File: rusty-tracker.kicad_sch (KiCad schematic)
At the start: 174 parts, among them J1 SIM8051-6-0-14-01-X, J2 USB_C_Receptacle_USB2.0, J3 NFC, J4 tag-connect-swd, J5 Battery Connector, Q1 BC846, Q2 BC846, SW1 SW_Push, T1 Tab, T2 Tab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

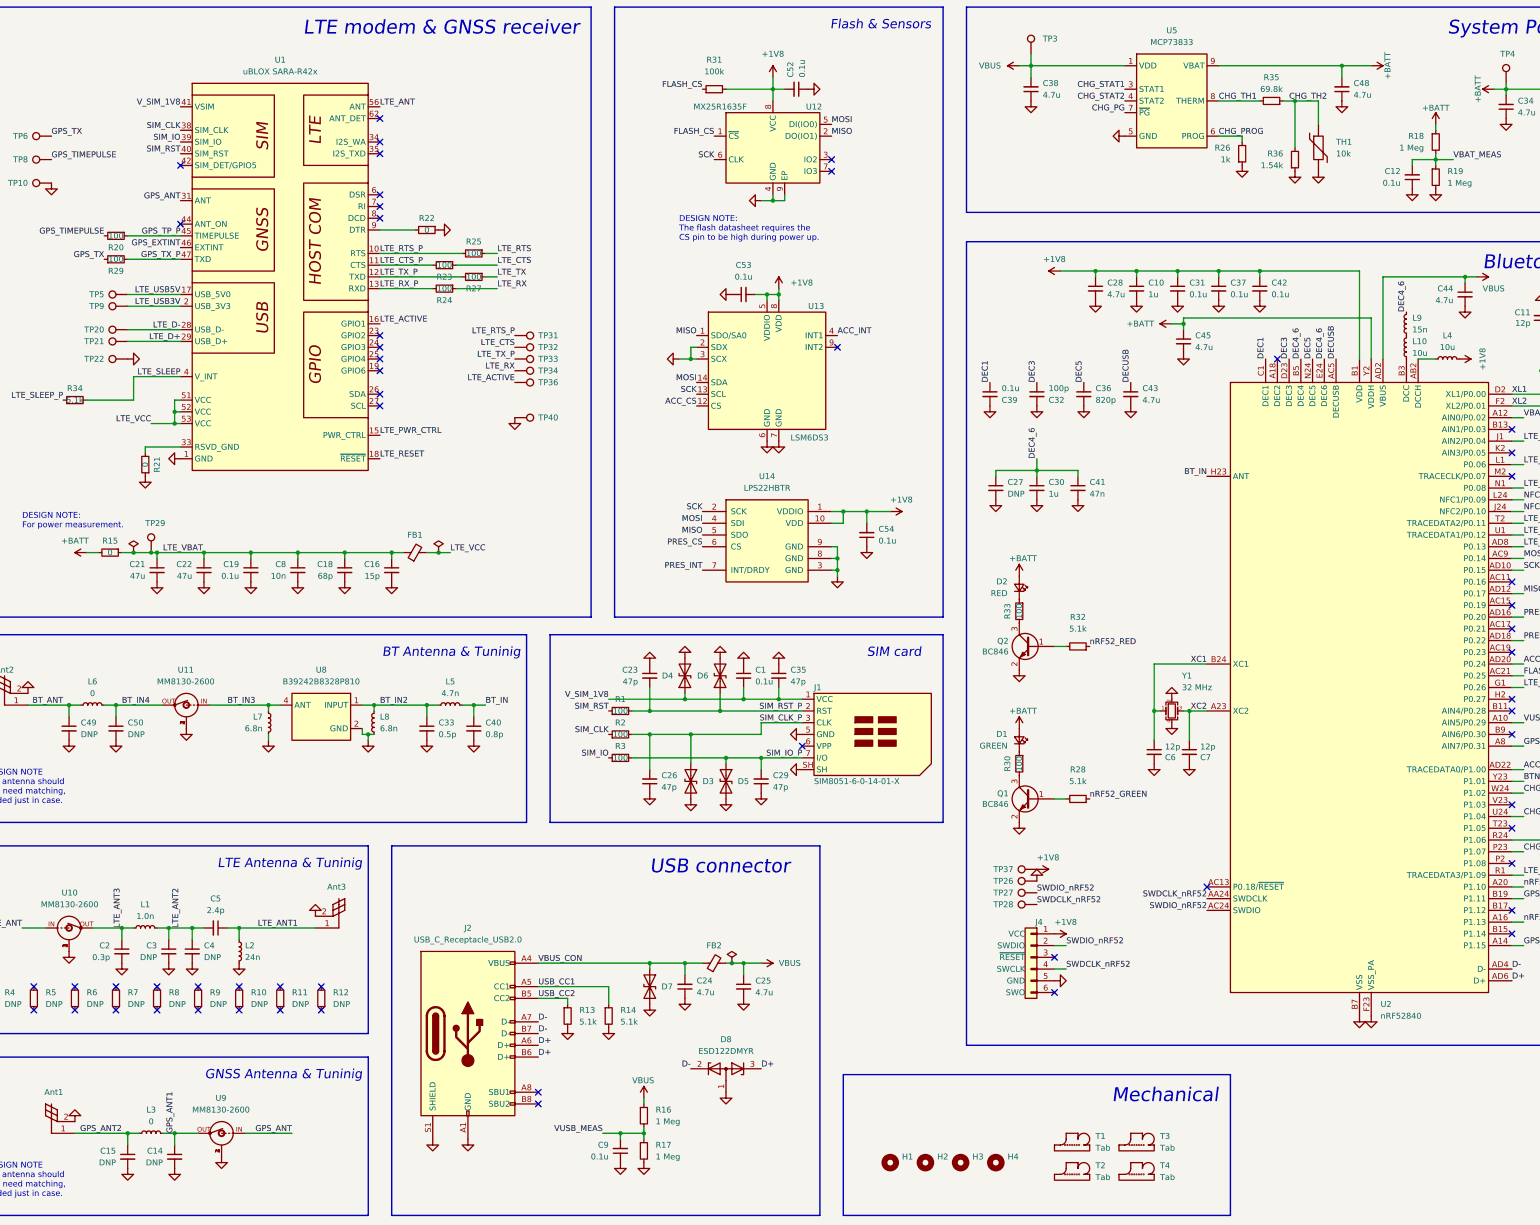
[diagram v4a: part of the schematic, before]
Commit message: Fix swapped thermistor resistors
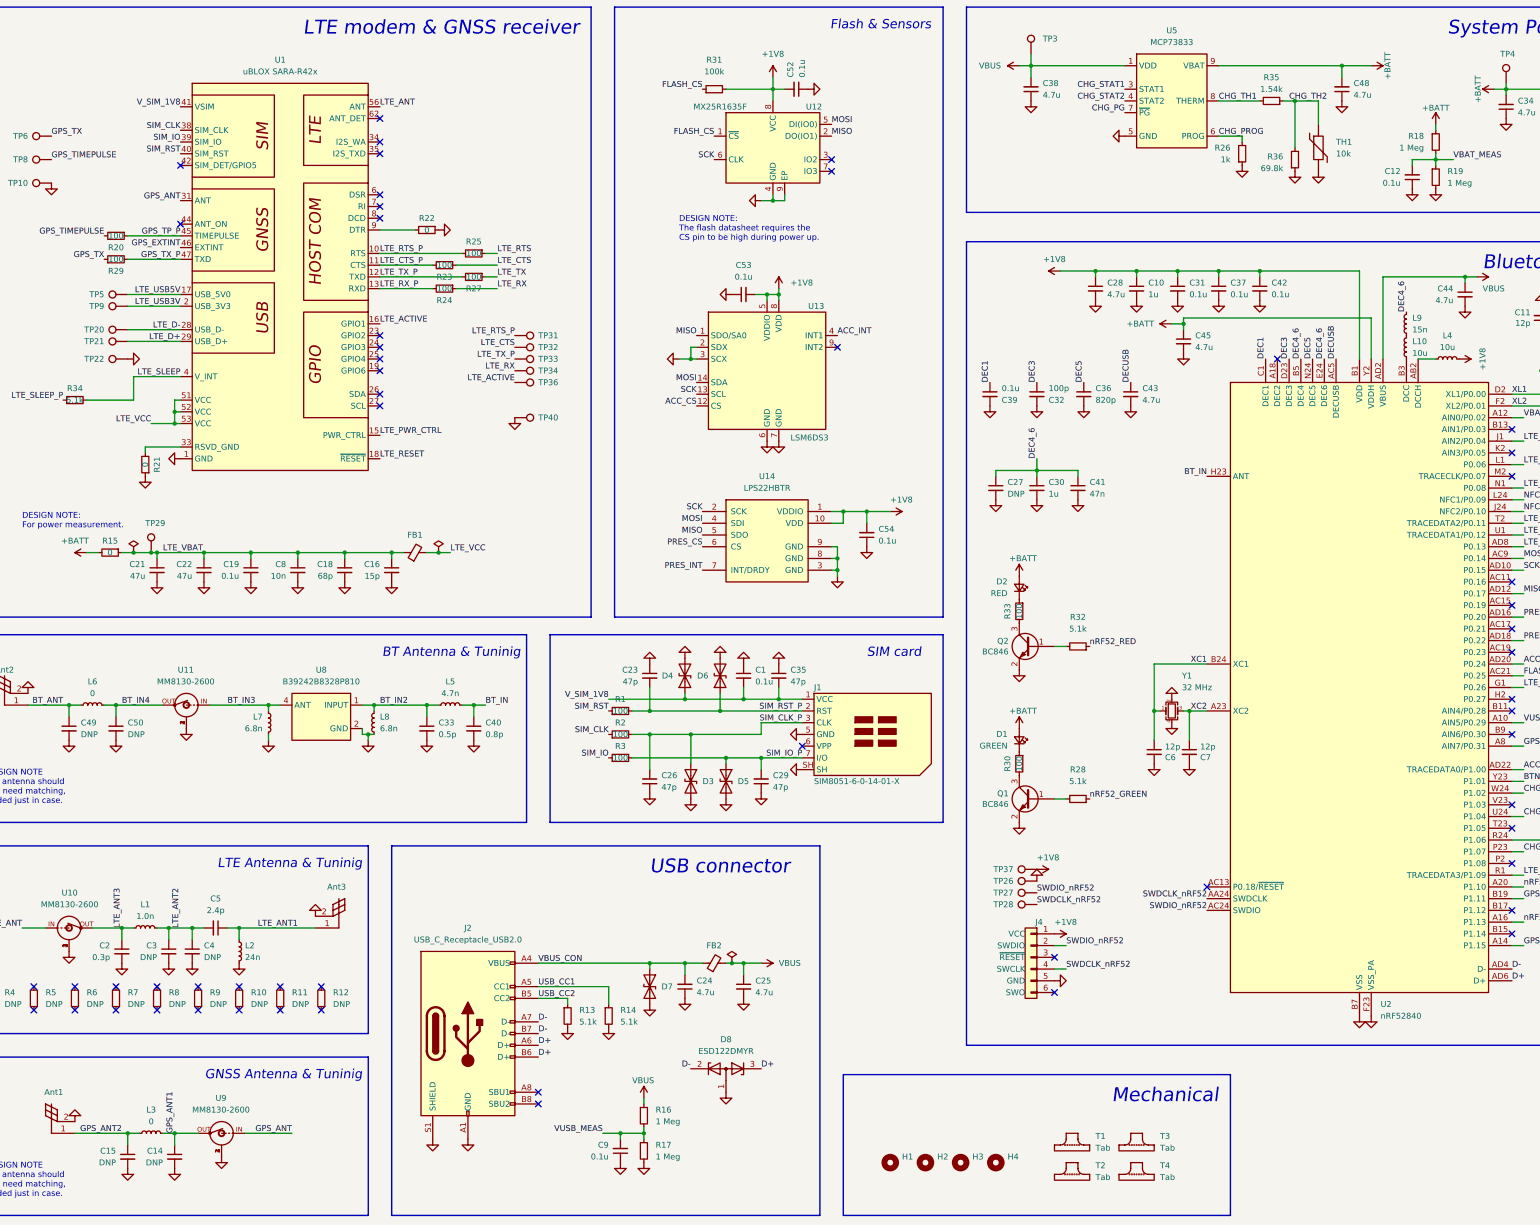
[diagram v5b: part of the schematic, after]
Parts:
- R35: value 69.8k -> 1.54k
- R36: value 1.54k -> 69.8k

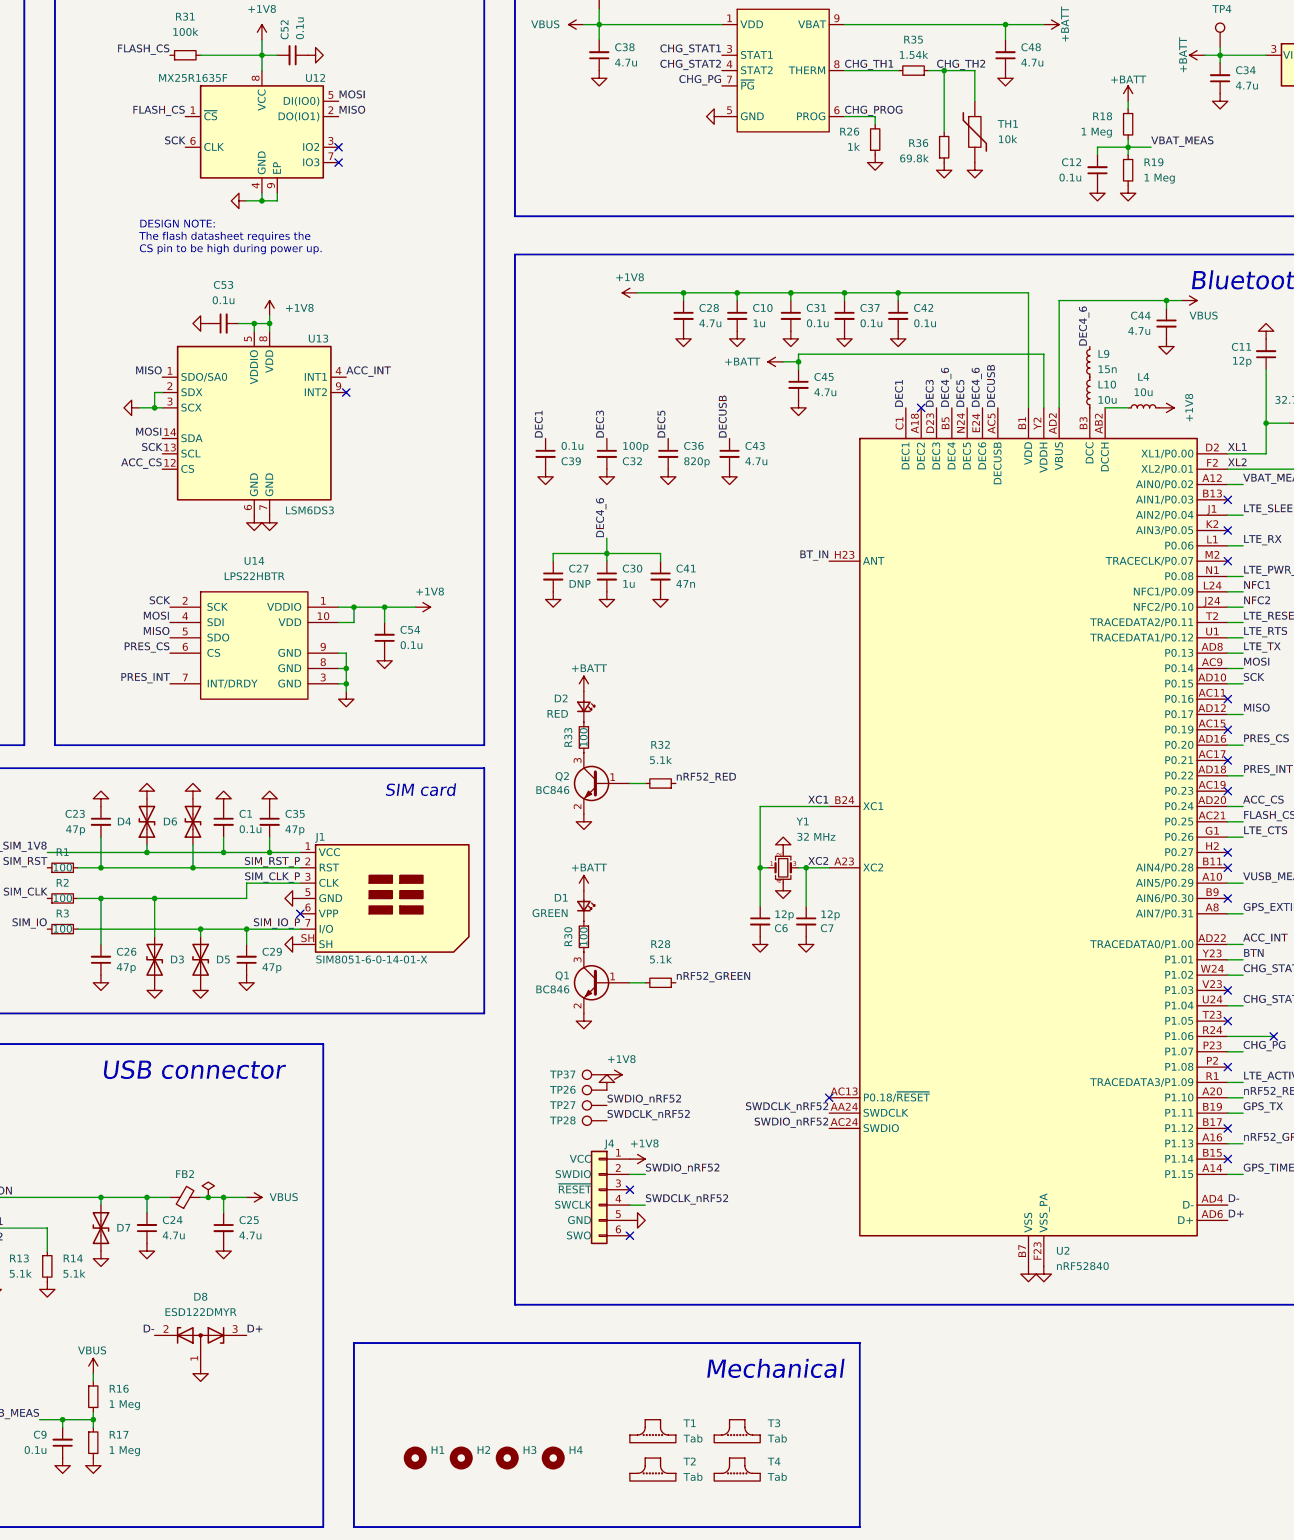
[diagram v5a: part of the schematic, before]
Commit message: Update ADC resistor divider values
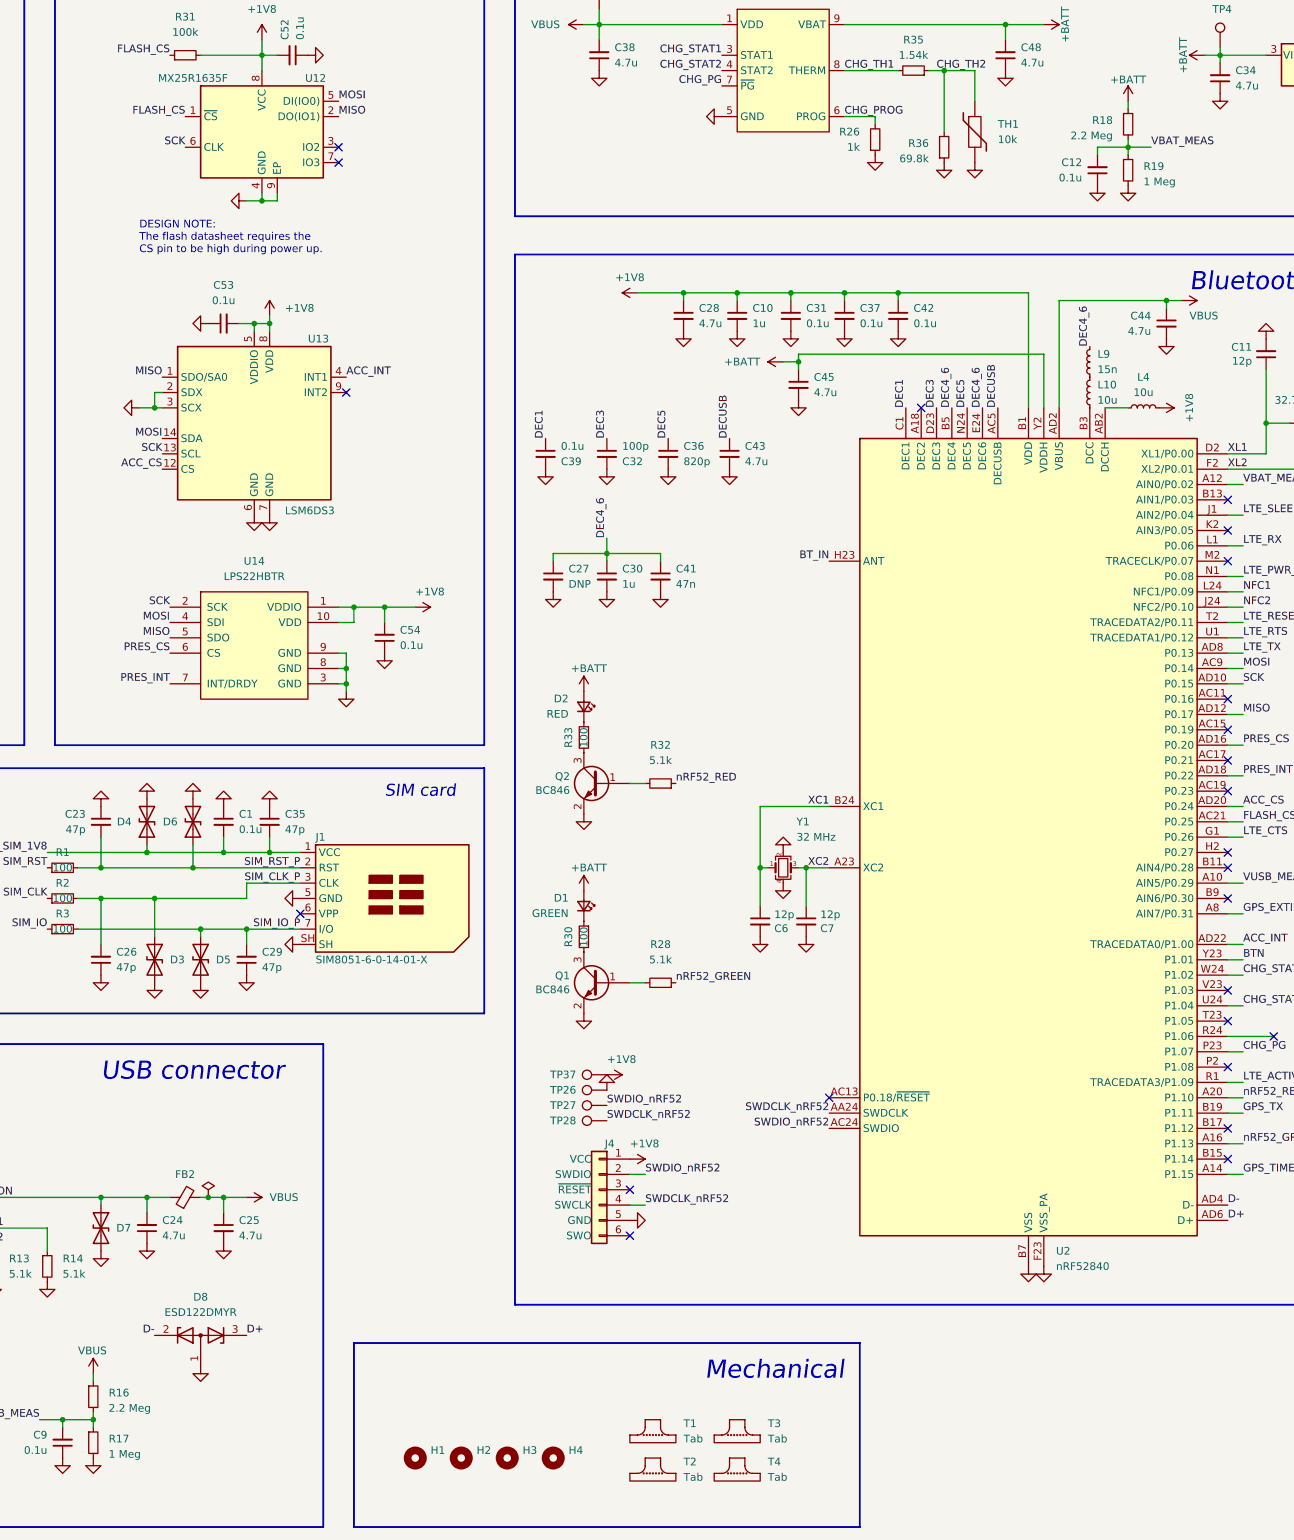
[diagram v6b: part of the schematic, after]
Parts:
- R16, R18: value 1 Meg -> 2.2 Meg
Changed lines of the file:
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@@
   (symbol (lib_id "Device:R_Small") (at 336.55 44.45 0) (unit 1)
     (in_bom yes) (on_board yes) (dnp no) (fields_autoplaced)
-    (property "Reference" "R18" (at 334.01 43.1799 0)
+    (property "Reference" "R18" (at 334.01 43.815 0)
       (effects (font (size 1.27 1.27)) (justify right))
     )
-    (property "Value" "1 Meg" (at 334.01 45.7199 0)
+    (property "Value" "2.2 Meg" (at 334.01 46.355 0)
       (effects (font (size 1.27 1.27)) (justify right))
     )
@@
   (symbol (lib_id "Device:R_Small") (at 165.1 255.27 0) (unit 1)
     (in_bom yes) (on_board yes) (dnp no) (fields_autoplaced)
-    (property "Reference" "R16" (at 167.64 253.9999 0)
+    (property "Reference" "R16" (at 167.64 254.635 0)
       (effects (font (size 1.27 1.27)) (justify left))
     )
-    (property "Value" "1 Meg" (at 167.64 256.5399 0)
+    (property "Value" "2.2 Meg" (at 167.64 257.175 0)
       (effects (font (size 1.27 1.27)) (justify left))
     )
@@
   (symbol (lib_id "Device:R_Small") (at 336.55 52.07 0) (unit 1)
     (in_bom yes) (on_board yes) (dnp no) (fields_autoplaced)
-    (property "Reference" "R19" (at 339.09 50.7999 0)
+    (property "Reference" "R19" (at 339.09 51.435 0)
       (effects (font (size 1.27 1.27)) (justify left))
     )
-    (property "Value" "1 Meg" (at 339.09 53.3399 0)
+    (property "Value" "1 Meg" (at 339.09 53.975 0)
       (effects (font (size 1.27 1.27)) (justify left))
     )
@@
   (symbol (lib_id "Device:R_Small") (at 165.1 262.89 0) (unit 1)
     (in_bom yes) (on_board yes) (dnp no) (fields_autoplaced)
-    (property "Reference" "R17" (at 167.64 261.6199 0)
+    (property "Reference" "R17" (at 167.64 262.255 0)
       (effects (font (size 1.27 1.27)) (justify left))
     )
-    (property "Value" "1 Meg" (at 167.64 264.1599 0)
+    (property "Value" "1 Meg" (at 167.64 264.795 0)
       (effects (font (size 1.27 1.27)) (justify left))
     )
